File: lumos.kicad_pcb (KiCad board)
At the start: 2 copper layers, 35.6 x 21.6 mm, 8 parts, among them CON1 BARREL_JACK, IC1 ATTINY85-P, P1 LDP8806, P2 SPI, SW1 SW_PUSH

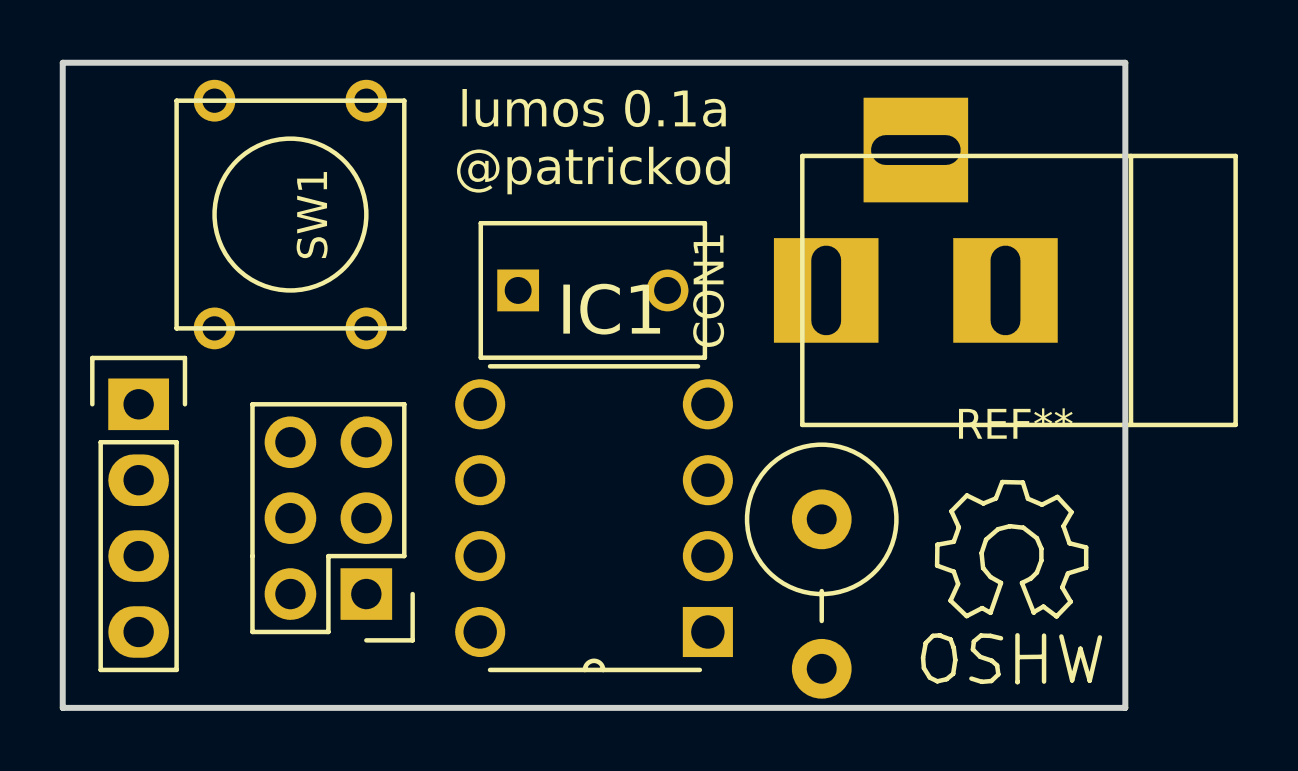
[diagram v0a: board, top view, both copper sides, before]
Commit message: PCB w/ traces, silk screening, updated ground on barrel jack
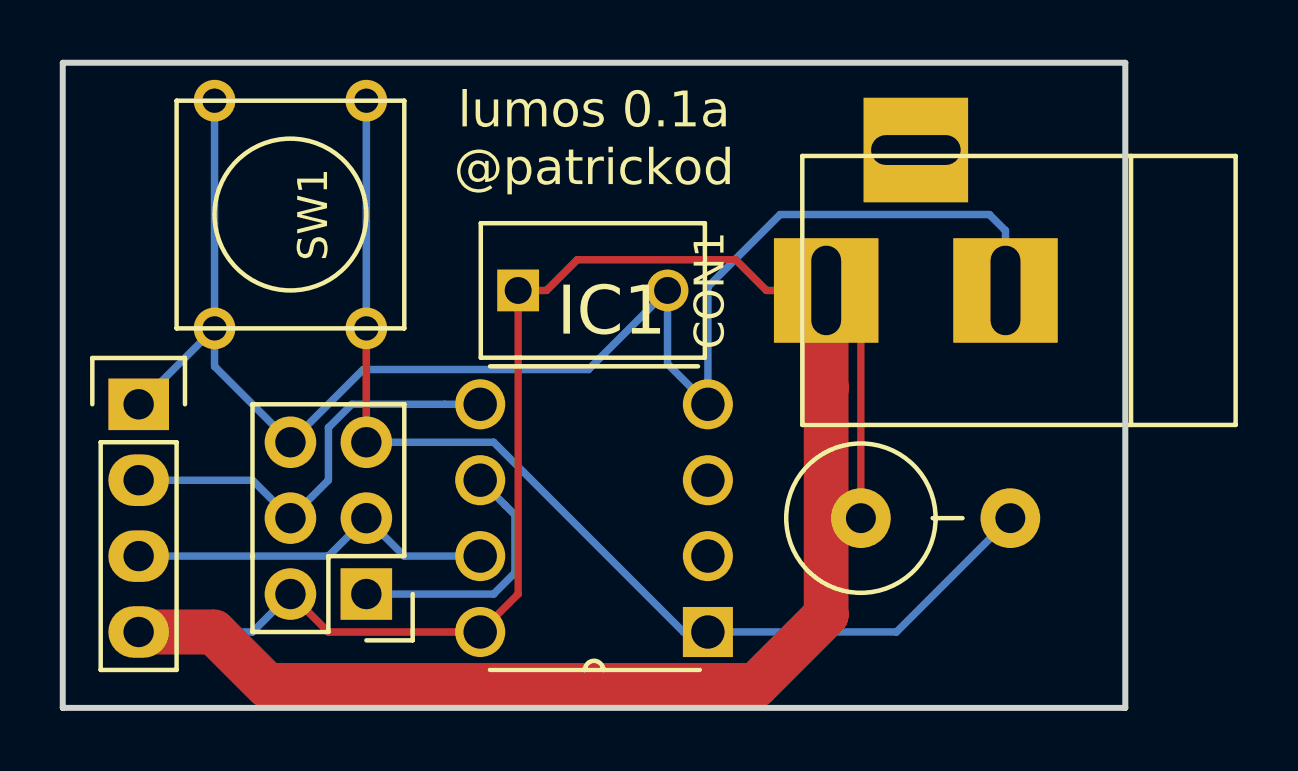
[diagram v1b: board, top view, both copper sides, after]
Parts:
- REF**: moved to B.Cu
- moved REF** 17.3 mm to (157.5, 95.2), turned to 180 degrees
- moved R1 4.58 mm to (165.1, 108.0), turned to 0 degrees
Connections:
- CON1 pad 3: Net-(CON1-Pad3) -> GND
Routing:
- net +5V: track 0.00 -> 79.5 mm
- net GND: track 0.00 -> 52.3 mm
- net /RST: track 0.00 -> 37.2 mm
- net /MOSI: track 0.00 -> 14.6 mm
- net /SCK: track 0.00 -> 12.5 mm
- net /MISO: track 0.00 -> 8.85 mm
- added copper zone on B.Cu, net +5V
- added copper zone on F.Cu, net GND
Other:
- board text added: "v0.1a 2/4/16 GPLv3"
